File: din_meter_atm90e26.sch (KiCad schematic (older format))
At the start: 38 parts, among them J1 USEL, J2 MMD1, J3 MMD0, J4 CONN_02X18, J5 CONN_01X10, J6 USEL, J7 MMD1, J8 MMD0, M1 ATM90E26_ATM90E26, M2 ATM90E26_ATM90E26, Y1 Crystal_Small, Y2 Crystal_Small

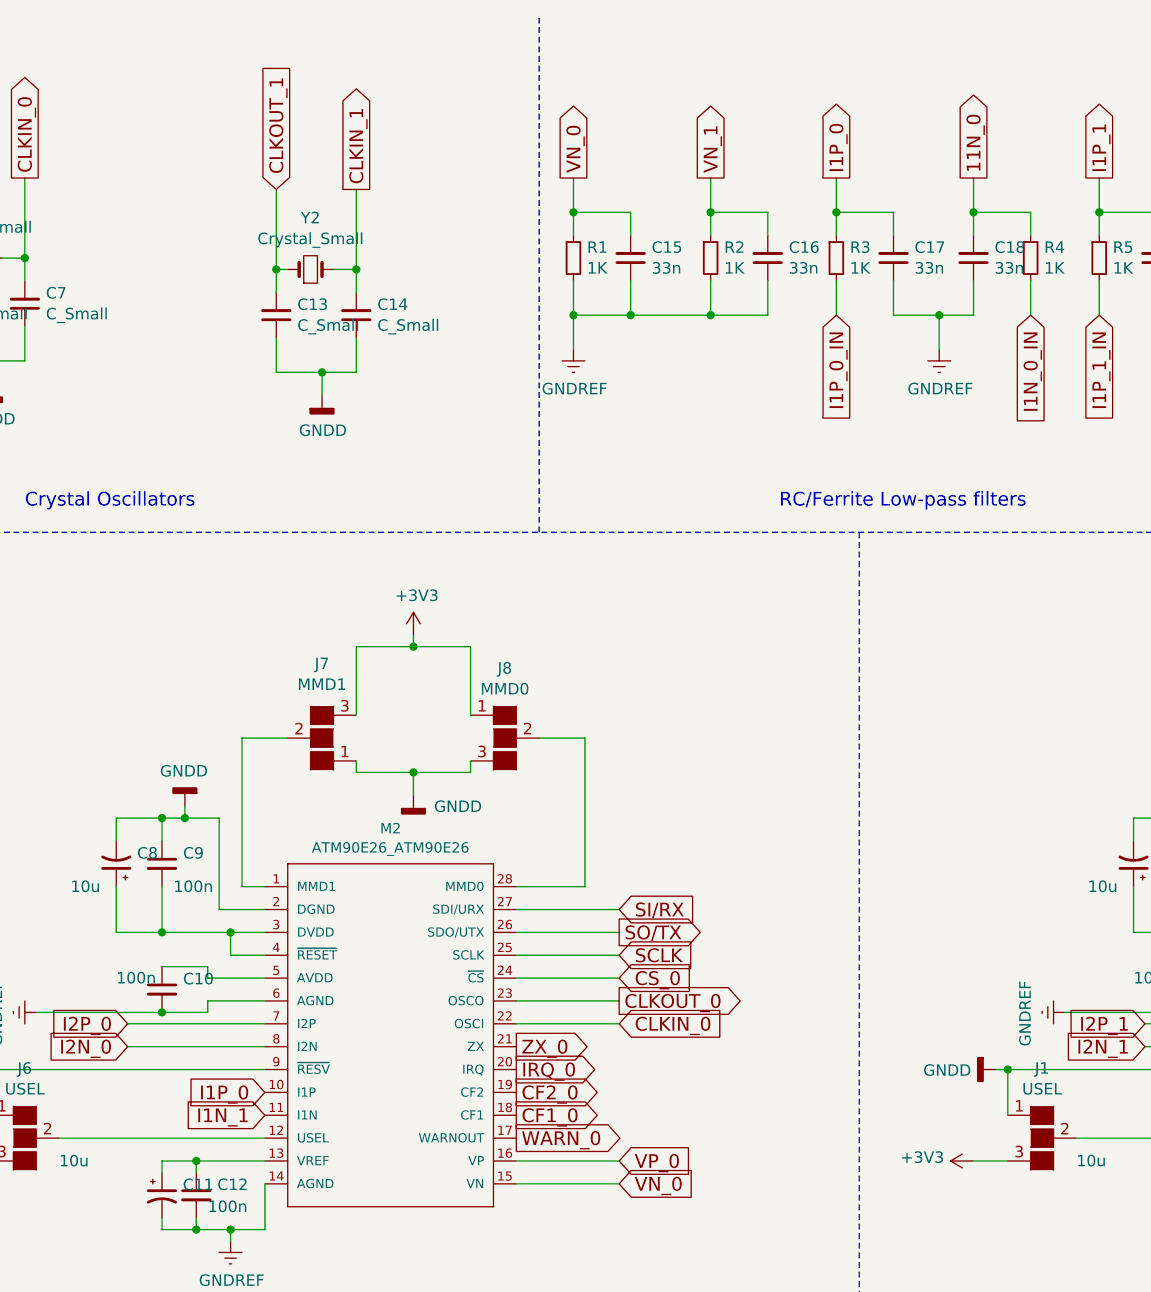
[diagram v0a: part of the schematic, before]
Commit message: Initial place and route without PCI-E connector
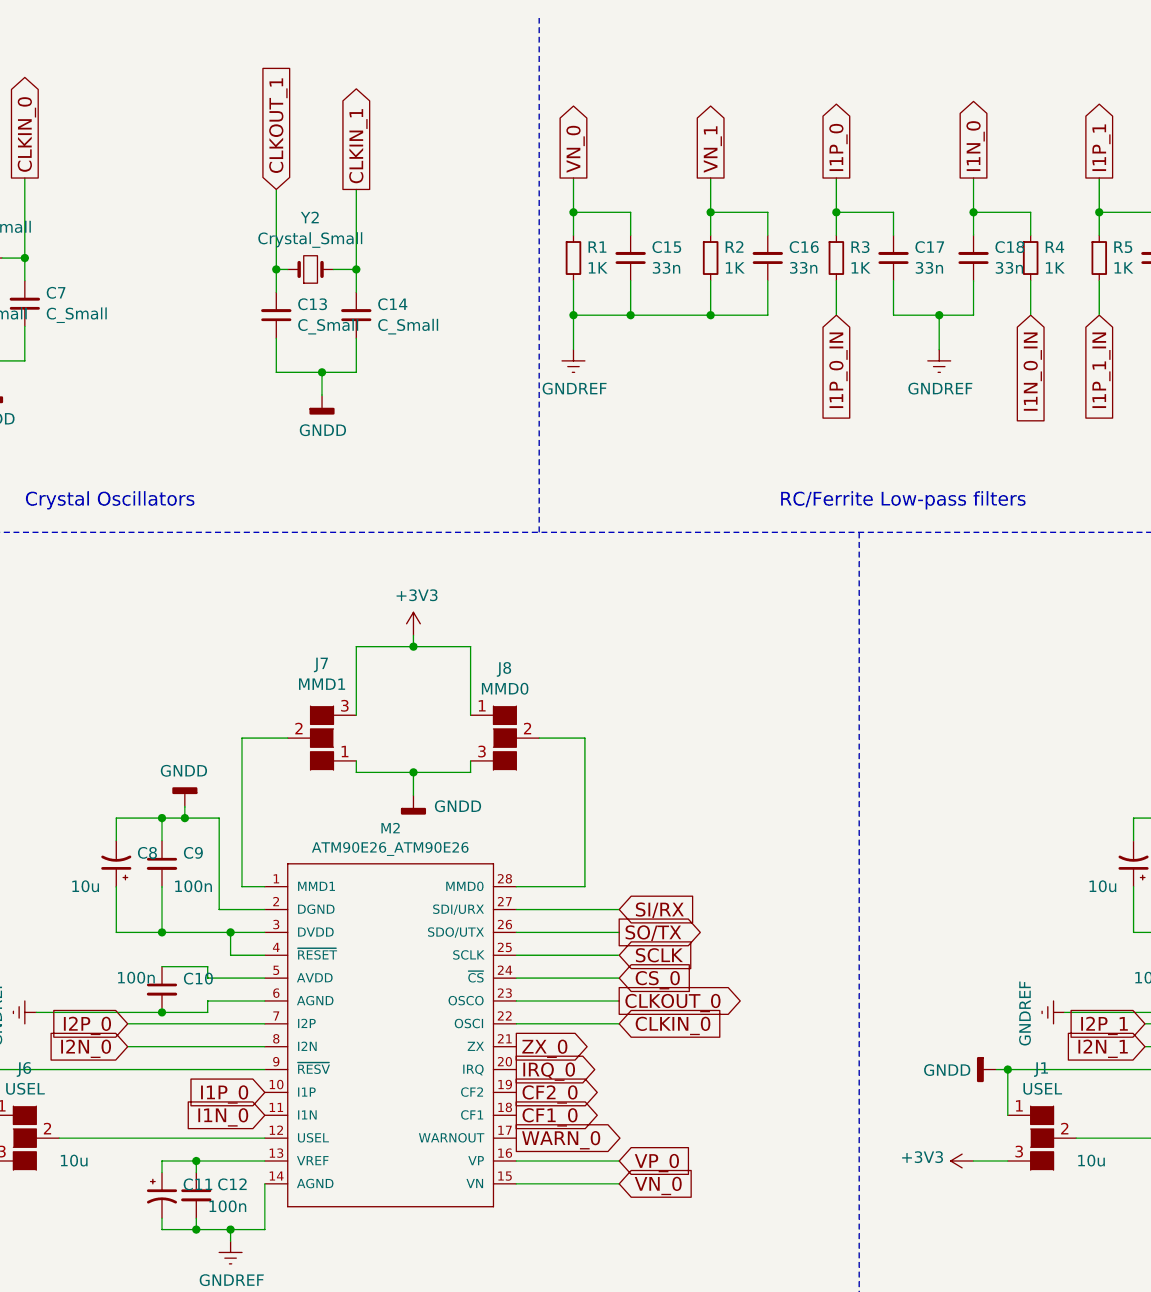
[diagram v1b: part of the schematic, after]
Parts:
- Y1, Y2: footprint Crystals:Crystal_SMD_3225-4pin_3.2x2.5mm -> Crystals:Crystal_SMD_5032-2pin_5.0x3.2mm
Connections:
- net labels added: I1N_0
- net labels removed: 11N_0
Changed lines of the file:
@@
 $EndComp
 $Comp
-L GNDREF #PWR17
+L GNDREF #PWR01
 U 1 1 59C723F8
 P 6900 5800
-F 0 "#PWR17" H 6900 5550 50  0001 C CNN
+F 0 "#PWR01" H 6900 5550 50  0001 C CNN
 F 1 "GNDREF" H 6905 5627 50  0000 C CNN
 F 2 "" H 6900 5800 50  0001 C CNN
@@
 $EndComp
 $Comp
-L GNDD #PWR13
+L GNDD #PWR02
 U 1 1 59C724CB
 P 5800 5050
-F 0 "#PWR13" H 5800 4800 50  0001 C CNN
+F 0 "#PWR02" H 5800 4800 50  0001 C CNN
 F 1 "GNDD" V 5804 4940 50  0000 R CNN
 F 2 "" H 5800 5050 50  0001 C CNN
@@
 $EndComp
 $Comp
-L GNDD #PWR16
+L GNDD #PWR03
 U 1 1 59C725DC
 P 6700 3900
-F 0 "#PWR16" H 6700 3650 50  0001 C CNN
+F 0 "#PWR03" H 6700 3650 50  0001 C CNN
 F 1 "GNDD" H 6704 3745 50  0000 C CNN
 F 2 "" H 6700 3900 50  0001 C CNN
@@
 $EndComp
 $Comp
-L +3V3 #PWR18
+L +3V3 #PWR04
 U 1 1 59CBC5D9
 P 7700 3150
-F 0 "#PWR18" H 7700 3000 50  0001 C CNN
+F 0 "#PWR04" H 7700 3000 50  0001 C CNN
 F 1 "+3V3" H 7715 3323 50  0000 C CNN
 F 2 "" H 7700 3150 50  0001 C CNN
@@
 $EndComp
 $Comp
-L GNDD #PWR19
+L GNDD #PWR05
 U 1 1 59CBCA12
 P 7700 3850
-F 0 "#PWR19" H 7700 3600 50  0001 C CNN
+F 0 "#PWR05" H 7700 3600 50  0001 C CNN
 F 1 "GNDD" H 8000 3800 50  0000 R CNN
 F 2 "" H 7700 3850 50  0001 C CNN
@@
 $EndComp
 $Comp
-L +3V3 #PWR12
+L +3V3 #PWR06
 U 1 1 59CBCD65
 P 5700 5450
-F 0 "#PWR12" H 5700 5300 50  0001 C CNN
+F 0 "#PWR06" H 5700 5300 50  0001 C CNN
 F 1 "+3V3" V 5715 5578 50  0000 L CNN
 F 2 "" H 5700 5450 50  0001 C CNN
@@
 F 0 "Y1" H 1350 1725 50  0000 C CNN
 F 1 "Crystal_Small" H 1350 1634 50  0000 C CNN
-F 2 "Crystals:Crystal_SMD_3225-4pin_3.2x2.5mm" H 1350 1500 50  0001 C CNN
+F 2 "Crystals:Crystal_SMD_5032-2pin_5.0x3.2mm" H 1350 1500 50  0001 C CNN
 F 3 "" H 1350 1500 50  0001 C CNN
 	1    1350 1500
@@
 $EndComp
 $Comp
-L GNDD #PWR3
+L GNDD #PWR07
 U 1 1 59D4F1BA
 P 1400 2050
-F 0 "#PWR3" H 1400 1800 50  0001 C CNN
+F 0 "#PWR07" H 1400 1800 50  0001 C CNN
 F 1 "GNDD" H 1404 1895 50  0000 C CNN
 F 2 "" H 1400 2050 50  0001 C CNN
@@
 F 0 "Y2" H 2800 1775 50  0000 C CNN
 F 1 "Crystal_Small" H 2800 1684 50  0000 C CNN
-F 2 "Crystals:Crystal_SMD_3225-4pin_3.2x2.5mm" H 2800 1550 50  0001 C CNN
+F 2 "Crystals:Crystal_SMD_5032-2pin_5.0x3.2mm" H 2800 1550 50  0001 C CNN
 F 3 "" H 2800 1550 50  0001 C CNN
 	1    2800 1550
@@
 $EndComp
 $Comp
-L GNDD #PWR7
+L GNDD #PWR08
 U 1 1 59DB8281
 P 2850 2100
-F 0 "#PWR7" H 2850 1850 50  0001 C CNN
+F 0 "#PWR08" H 2850 1850 50  0001 C CNN
 F 1 "GNDD" H 2854 1945 50  0000 C CNN
 F 2 "" H 2850 2100 50  0001 C CNN
@@
 $EndComp
 $Comp
-L GNDREF #PWR6
+L GNDREF #PWR09
 U 1 1 59DB841C
 P 2450 5800
-F 0 "#PWR6" H 2450 5550 50  0001 C CNN
+F 0 "#PWR09" H 2450 5550 50  0001 C CNN
 F 1 "GNDREF" H 2455 5627 50  0000 C CNN
 F 2 "" H 2450 5800 50  0001 C CNN
@@
 $EndComp
 $Comp
-L GNDD #PWR2
+L GNDD #PWR010
 U 1 1 59DB8422
 P 1350 5050
-F 0 "#PWR2" H 1350 4800 50  0001 C CNN
+F 0 "#PWR010" H 1350 4800 50  0001 C CNN
 F 1 "GNDD" V 1354 4940 50  0000 R CNN
 F 2 "" H 1350 5050 50  0001 C CNN
@@
 $EndComp
 $Comp
-L GNDD #PWR5
+L GNDD #PWR011
 U 1 1 59DB8428
 P 2250 3900
-F 0 "#PWR5" H 2250 3650 50  0001 C CNN
+F 0 "#PWR011" H 2250 3650 50  0001 C CNN
 F 1 "GNDD" H 2254 3745 50  0000 C CNN
 F 2 "" H 2250 3900 50  0001 C CNN
@@
 $EndComp
 $Comp
-L +3V3 #PWR8
+L +3V3 #PWR012
 U 1 1 59DB843C
 P 3250 3150
-F 0 "#PWR8" H 3250 3000 50  0001 C CNN
+F 0 "#PWR012" H 3250 3000 50  0001 C CNN
 F 1 "+3V3" H 3265 3323 50  0000 C CNN
 F 2 "" H 3250 3150 50  0001 C CNN
@@
 $EndComp
 $Comp
-L GNDD #PWR9
+L GNDD #PWR013
 U 1 1 59DB8442
 P 3250 3850
-F 0 "#PWR9" H 3250 3600 50  0001 C CNN
+F 0 "#PWR013" H 3250 3600 50  0001 C CNN
 F 1 "GNDD" H 3550 3800 50  0000 R CNN
 F 2 "" H 3250 3850 50  0001 C CNN
@@
 $EndComp
 $Comp
-L +3V3 #PWR1
+L +3V3 #PWR014
 U 1 1 59DB848C
 P 1250 5450
-F 0 "#PWR1" H 1250 5300 50  0001 C CNN
+F 0 "#PWR014" H 1250 5300 50  0001 C CNN
 F 1 "+3V3" V 1265 5578 50  0000 L CNN
 F 2 "" H 1250 5450 50  0001 C CNN
@@
 I1P_0
 Text GLabel 2600 5250 0    60   Input ~ 0
-I1N_1
+I1N_0
 Text GLabel 3700 4950 2    60   Output ~ 0
 ZX_0
@@
 RC/Ferrite Low-pass filters
 $Comp
-L GNDREF #PWR4
+L GNDREF #PWR015
 U 1 1 59DD639C
 P 1600 4800
-F 0 "#PWR4" H 1600 4550 50  0001 C CNN
+F 0 "#PWR015" H 1600 4550 50  0001 C CNN
 F 1 "GNDREF" H 1605 4627 50  0000 C CNN
 F 2 "" H 1600 4800 50  0001 C CNN
@@
 $EndComp
 $Comp
-L GNDREF #PWR14
+L GNDREF #PWR016
 U 1 1 59DD6FBD
 P 6100 4800
-F 0 "#PWR14" H 6100 4550 50  0001 C CNN
+F 0 "#PWR016" H 6100 4550 50  0001 C CNN
 F 1 "GNDREF" H 6105 4627 50  0000 C CNN
 F 2 "" H 6100 4800 50  0001 C CNN
@@
 	4550 1600 4550 1750
 $Comp
-L GNDREF #PWR10
+L GNDREF #PWR017
 U 1 1 59DEBFFC
 P 3950 1900
-F 0 "#PWR10" H 3950 1650 50  0001 C CNN
+F 0 "#PWR017" H 3950 1650 50  0001 C CNN
 F 1 "GNDREF" H 3955 1727 50  0000 C CNN
 F 2 "" H 3950 1900 50  0001 C CNN
@@
 	5700 1600 5700 1750
 $Comp
-L GNDREF #PWR11
+L GNDREF #PWR018
 U 1 1 59DED841
 P 5550 1900
-F 0 "#PWR11" H 5550 1650 50  0001 C CNN
+F 0 "#PWR018" H 5550 1650 50  0001 C CNN
 F 1 "GNDREF" H 5555 1727 50  0000 C CNN
 F 2 "" H 5550 1900 50  0001 C CNN
@@
 I1P_0
 Text GLabel 5700 1150 1    60   Output ~ 0
-11N_0
+I1N_0
 $Comp
 L R_Small R6
@@
 	6850 1600 6850 1750
 $Comp
-L GNDREF #PWR15
+L GNDREF #PWR019
 U 1 1 59DEDB59
 P 6700 1950
-F 0 "#PWR15" H 6700 1700 50  0001 C CNN
+F 0 "#PWR019" H 6700 1700 50  0001 C CNN
 F 1 "GNDREF" H 6705 1777 50  0000 C CNN
 F 2 "" H 6700 1950 50  0001 C CNN

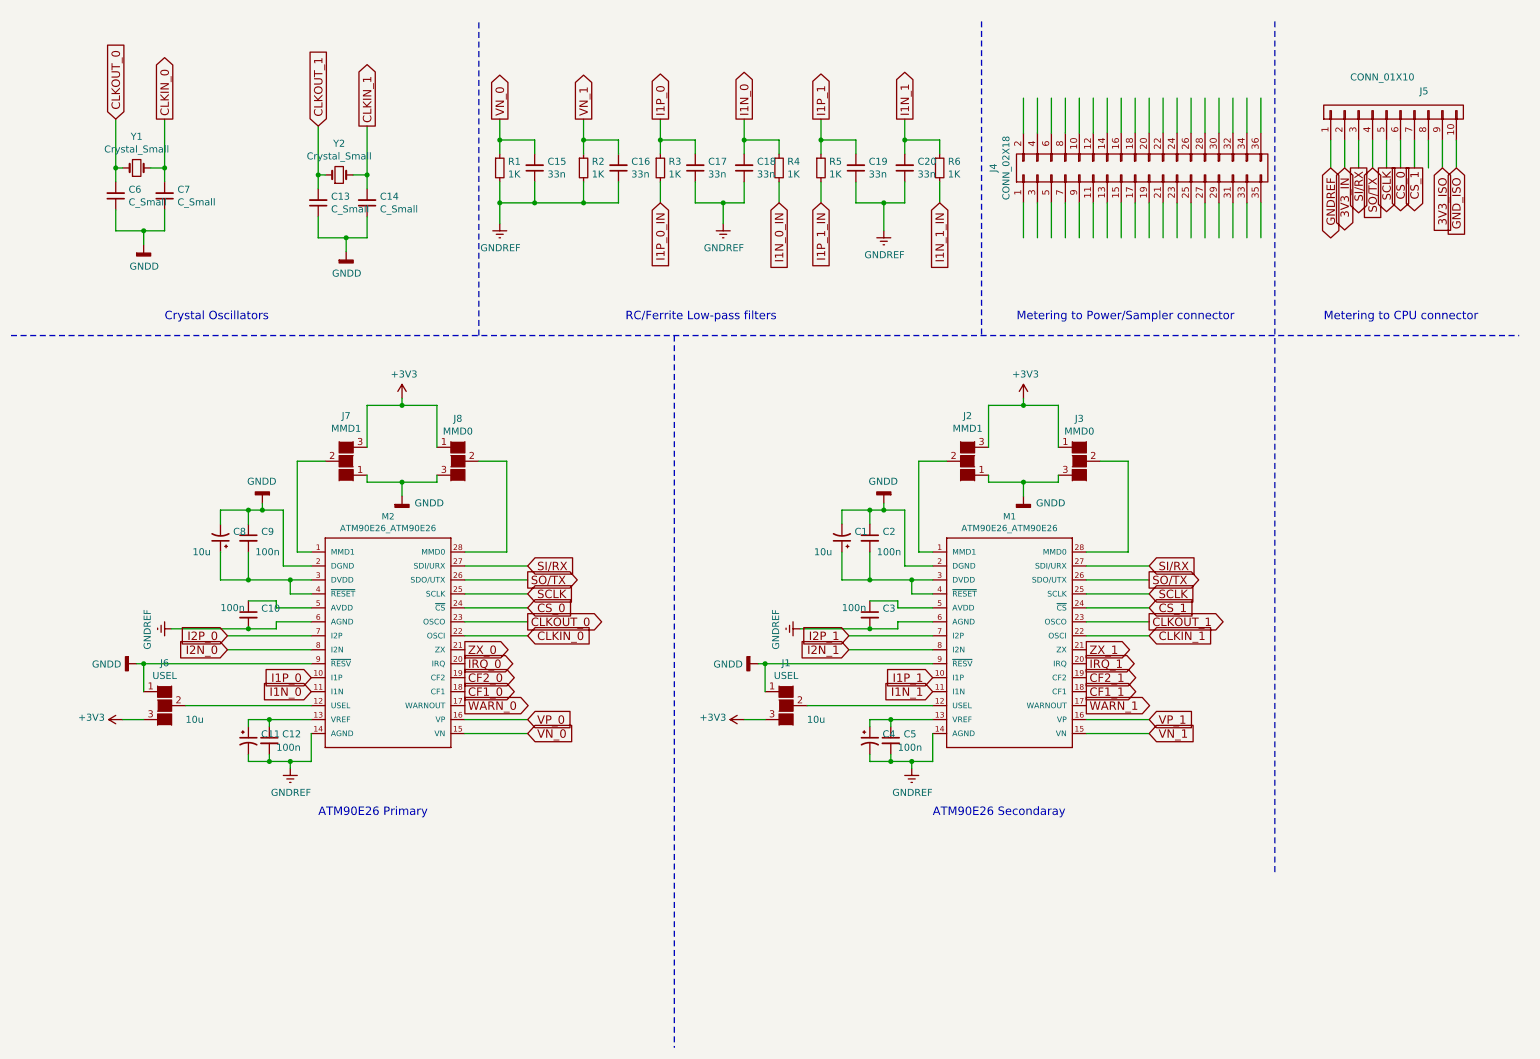
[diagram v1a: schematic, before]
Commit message: Initial place and route without PCI-E connector
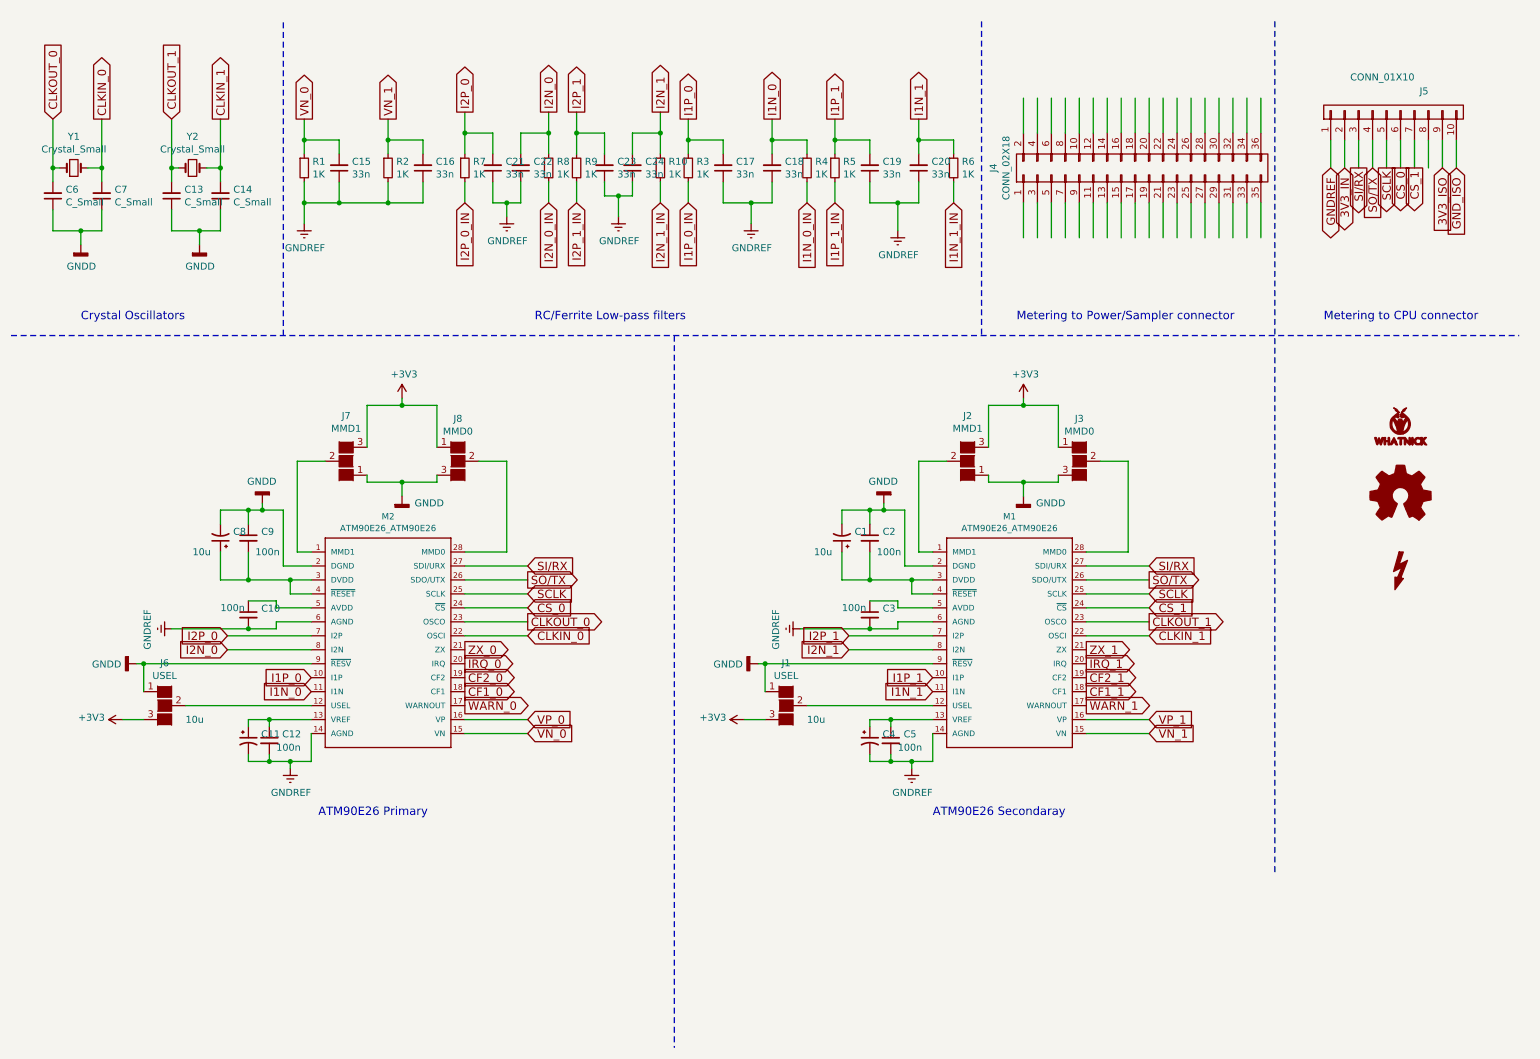
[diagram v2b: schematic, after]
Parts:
- added C21, C22, C23, C24: 33n, Capacitors_SMD:C_0402, symbol C_Small
- added G1: LOGO, Whatnick_logo:Whatnick_logo, symbol LOGO
- added LOGO1: Logo_Open_Hardware_Small, Symbols:OSHW-Logo2_7.3x6mm_SilkScreen, symbol Logo_Open_Hardware_Small
- added R10, R7, R8, R9: 1K, Resistors_SMD:R_0402, symbol R_Small
- added SYM1: SYM_Flash_Small, symbol SYM_Flash_Small
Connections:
- net labels added: I2N_0_IN, I2N_1_IN, I2P_0_IN, I2P_1_IN
- wire segments 203 -> 227
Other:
- moved on the sheet: C13, C14, C15, C16, C17, C18, C19, C20, C6, C7, R1, R2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

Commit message: Renumber PCI-X
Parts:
- J4: symbol CONN_02X18 -> PCIx1
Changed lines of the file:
@@
 CLKIN_1
 $Comp
-L CONN_02X18 J4
+L PCIx1 J4
 U 1 1 59CF9032
 P 8550 1500
